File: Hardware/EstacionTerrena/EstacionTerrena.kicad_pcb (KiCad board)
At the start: 2 copper layers, 40 x 30 mm, 63 parts, among them J1 5-1814832-1, J2 USB_B_Micro, J3 ICSP, U1 TPD2E2U06, U2 MIC5353-3.3YMT, U3 PIC18F14K50, U4 CC1101RGP, U5 0915BM15A0001E, U6 B39921B3588U410, U7 CC1190, Y1 12MHz, Y2 26 MHz

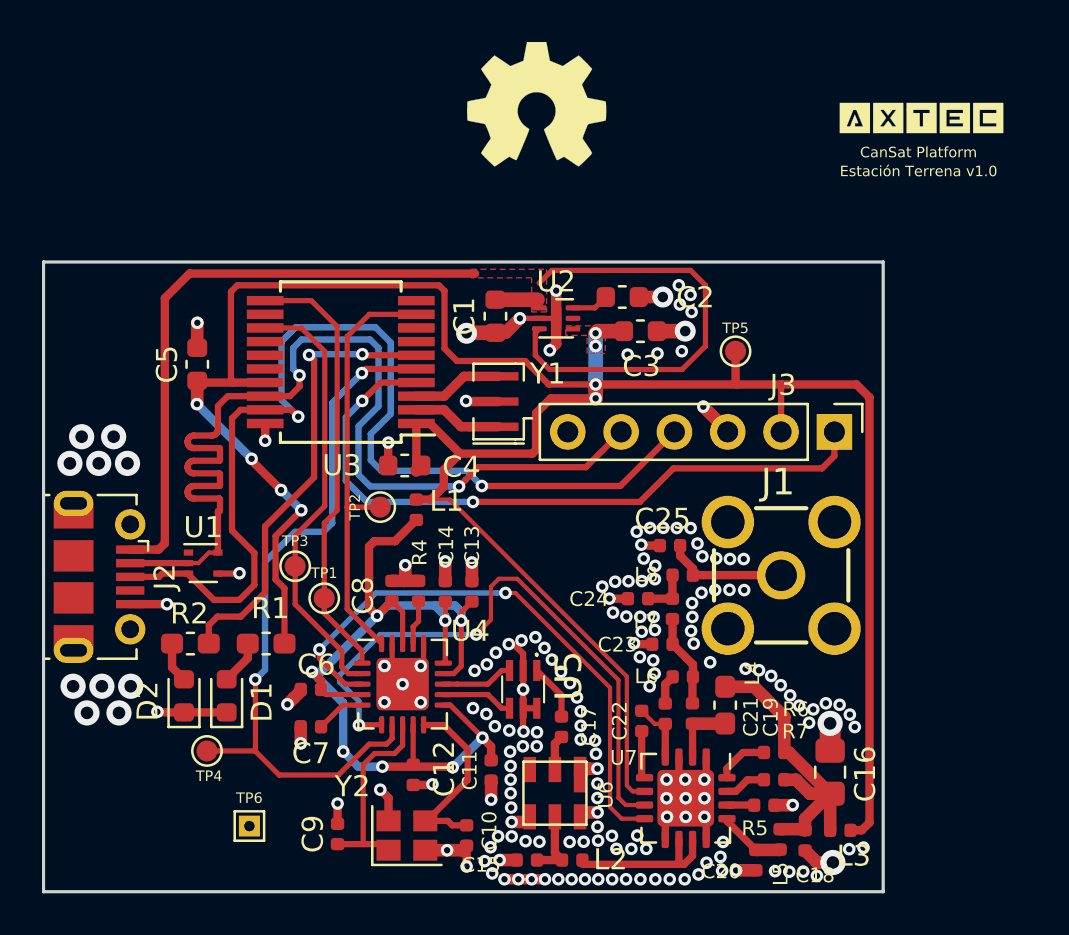
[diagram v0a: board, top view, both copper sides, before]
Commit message: Agregados silkscreen faltantes en estación terrena
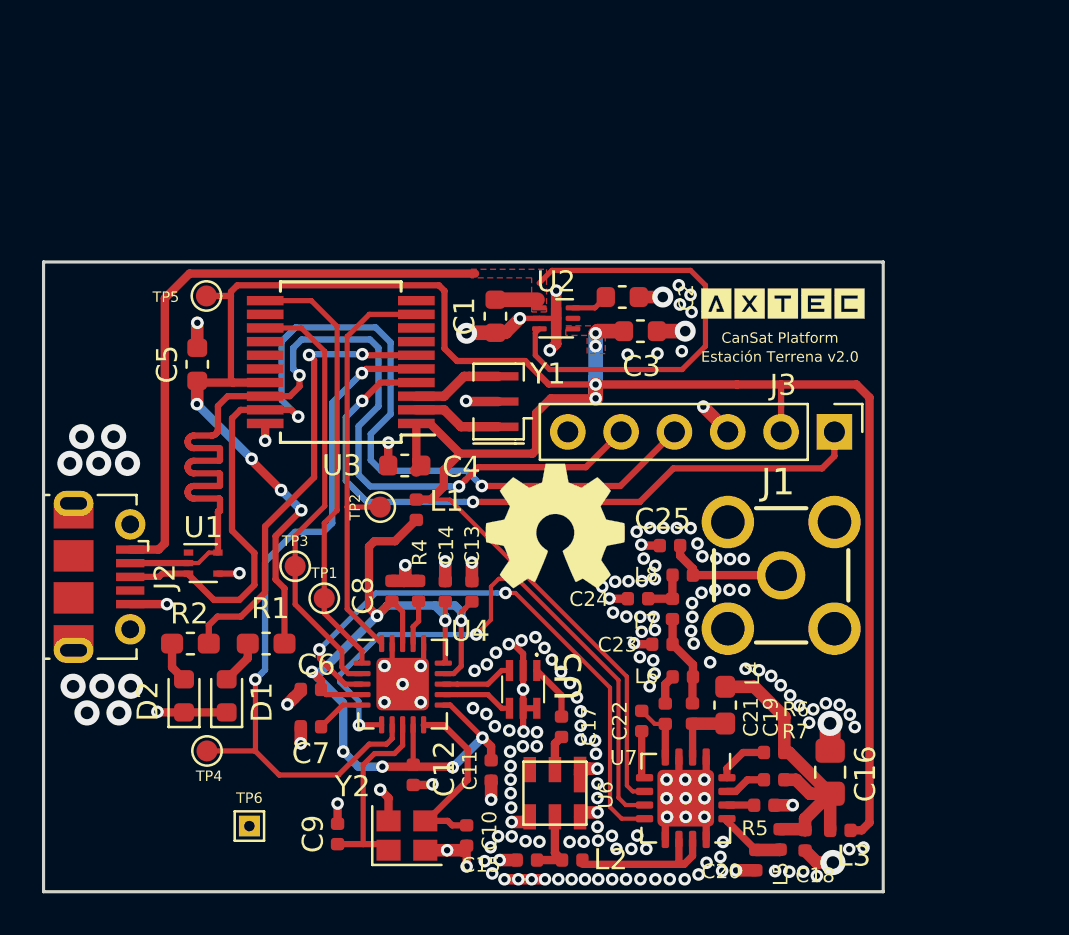
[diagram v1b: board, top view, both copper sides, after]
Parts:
- removed the G*** at (41.8, -7.06)
- removed the G*** at (41.9, -7.06)
- added G***: LOGO, AXTEC:Logo_AXTEC, B.Cu at (35.2, 1.78)
- added G***: LOGO, AXTEC:Logo_AXTEC, F.Cu at (35.3, 1.78)
- moved TP5 25.3 mm to (7.76, 1.62)
- moved REF** 21.0 mm to (24.4, 12.6)
- moved REF** 20.1 mm to (24.4, 12.6)
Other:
- board text added: "Estación Terrena v2.0"
- board text removed: "Estación Terrena v1.0"
